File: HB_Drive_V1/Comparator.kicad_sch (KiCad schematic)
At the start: 0 parts

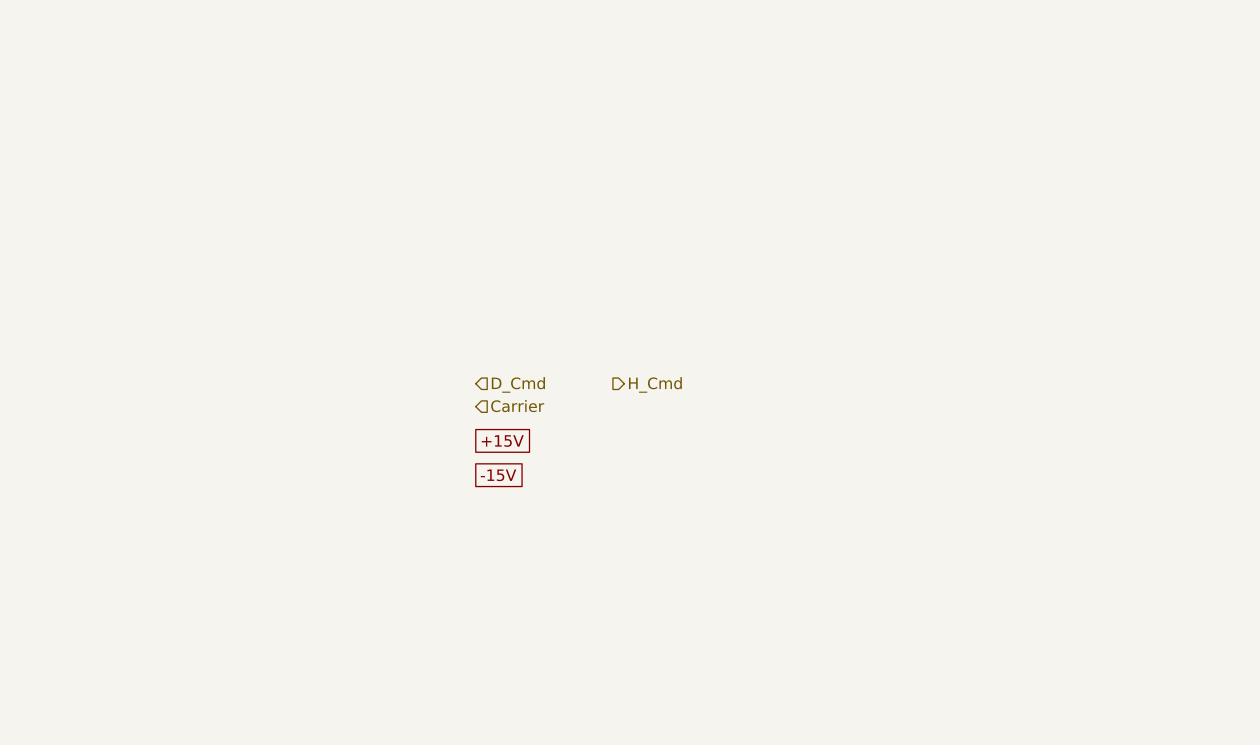
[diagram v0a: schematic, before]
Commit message: Adds Carrier Wave Circuit and Comparator Circuit
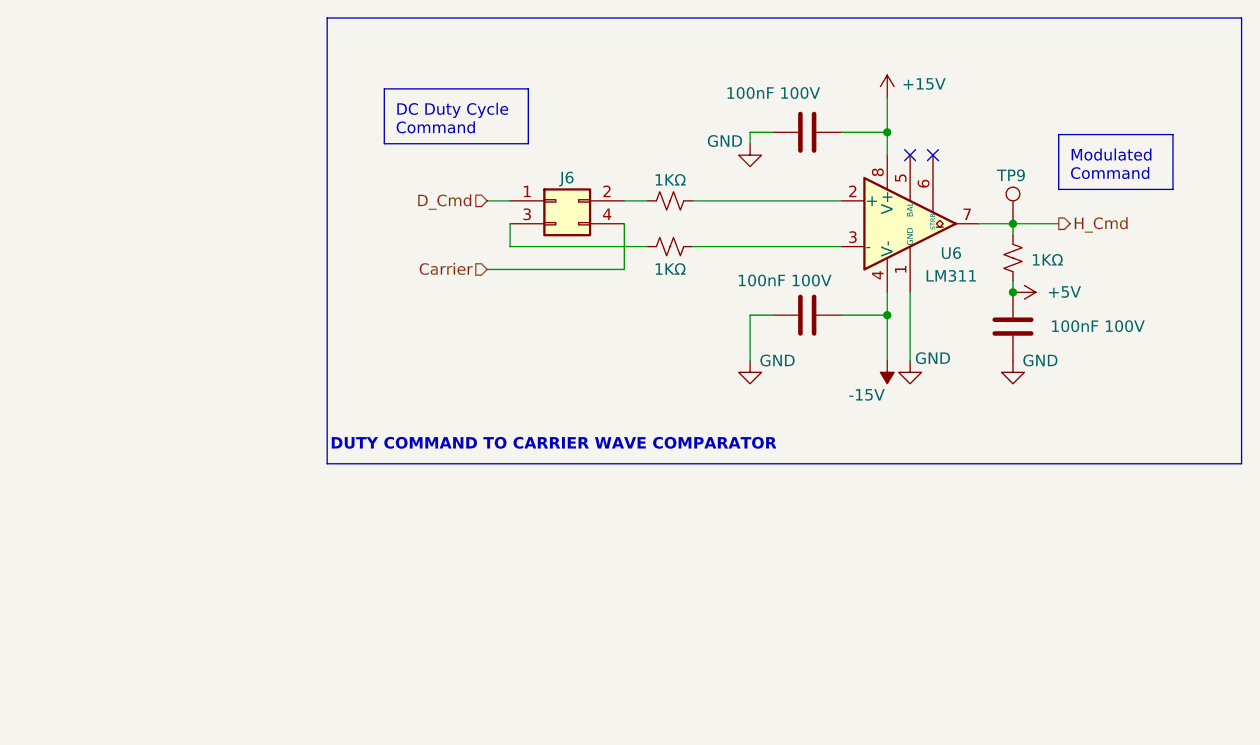
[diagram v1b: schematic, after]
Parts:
- added C22, C23, C24: 100nF 100V, Capacitor_SMD:C_0603_1608Metric, symbol Device:C
- added J6: Conn_02x02_Odd_Even, Connector_PinSocket_1.27mm:PinSocket_2x02_P1.27mm_Vertical, symbol Connector_Generic:Conn_02x02_Odd_Even
- added R41, R42, R43: 1KΩ, Resistor_SMD:R_0603_1608Metric_Pad0.98x0.95mm_HandSolder, symbol Device:R_Small_US
- added TP9: TestPoint, TestPoint:TestPoint_Loop_D2.60mm_Drill1.6mm_Beaded, symbol Connector:TestPoint
- added U6: LM311, symbol Comparator:LM311
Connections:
- net +15V: now also C22.1, U6.8 (V+)
- net -15V: now also C23.1, U6.4 (V-)
- net Carrier: now also J6.4 (Pin_4)
- net D_Cmd: now also J6.1 (Pin_1)
- net H_Cmd: now also R43.1, TP9.1, U6.7
- new net: J6.3 (Pin_3), R42.1
- new net: R42.2, U6.3 (-)
- new net: R41.2, U6.2 (+)
- new net: J6.2 (Pin_2), R41.1
- new net +5V: C24.2, R43.2
- new net GND: C22.2, C23.2, C24.1, U6.1 (GND)
- no-connect marks 0 -> 2
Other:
- note added: "DC Duty Cycle Command"
- note added: "DUTY COMMAND TO CARRIER WAVE COMPARATOR"
- note added: "Modulated Command"

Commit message: adds 10v reference and DC offsets / gain control to I_fdbk and V_fdbk
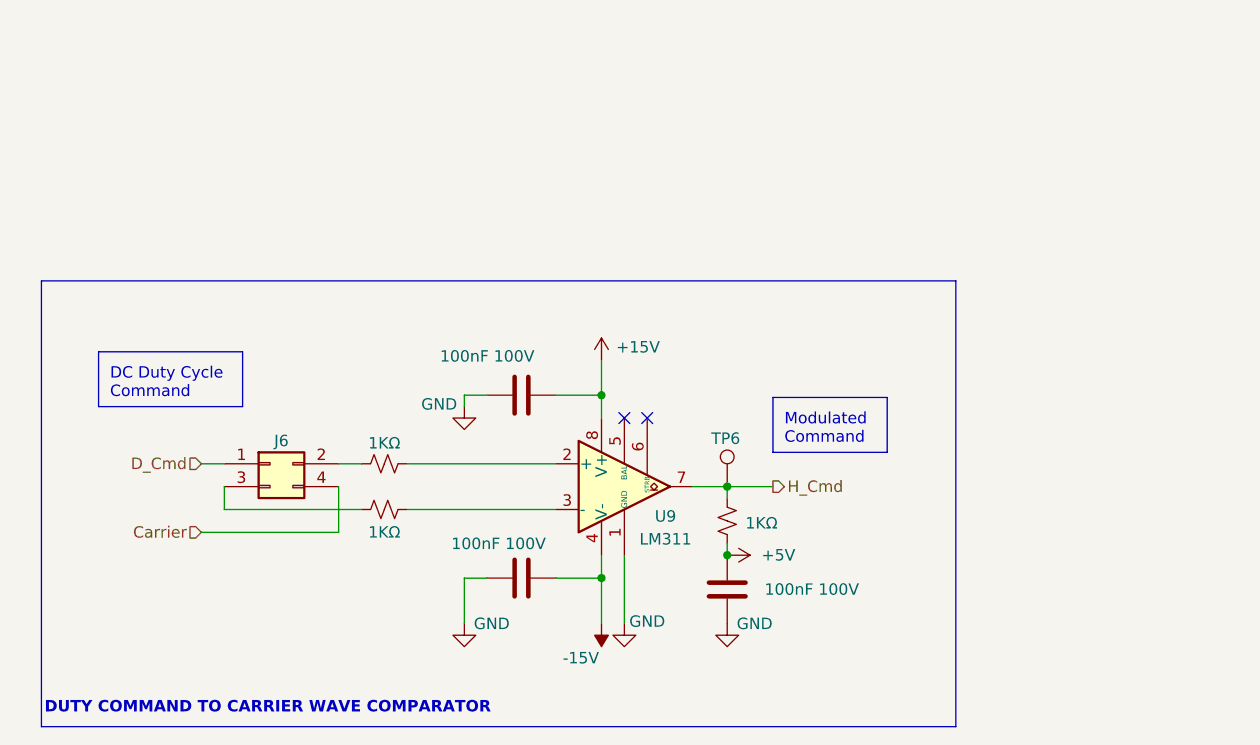
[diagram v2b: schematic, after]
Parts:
- renumbered C22 to C15, C23 to C16, C24 to C17, R41 to R32, R42 to R33, R43 to R34, TP9 to TP6, U6 to U9
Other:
- moved on the sheet: J6, TP6, U9
